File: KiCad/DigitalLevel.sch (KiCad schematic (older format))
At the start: 67 parts, among them SW1 SW_Push_Open, SW2 SW_Push_Open, SW3 SW_Push_Open, U2 MPU-6050, U3 XC6206P332MR

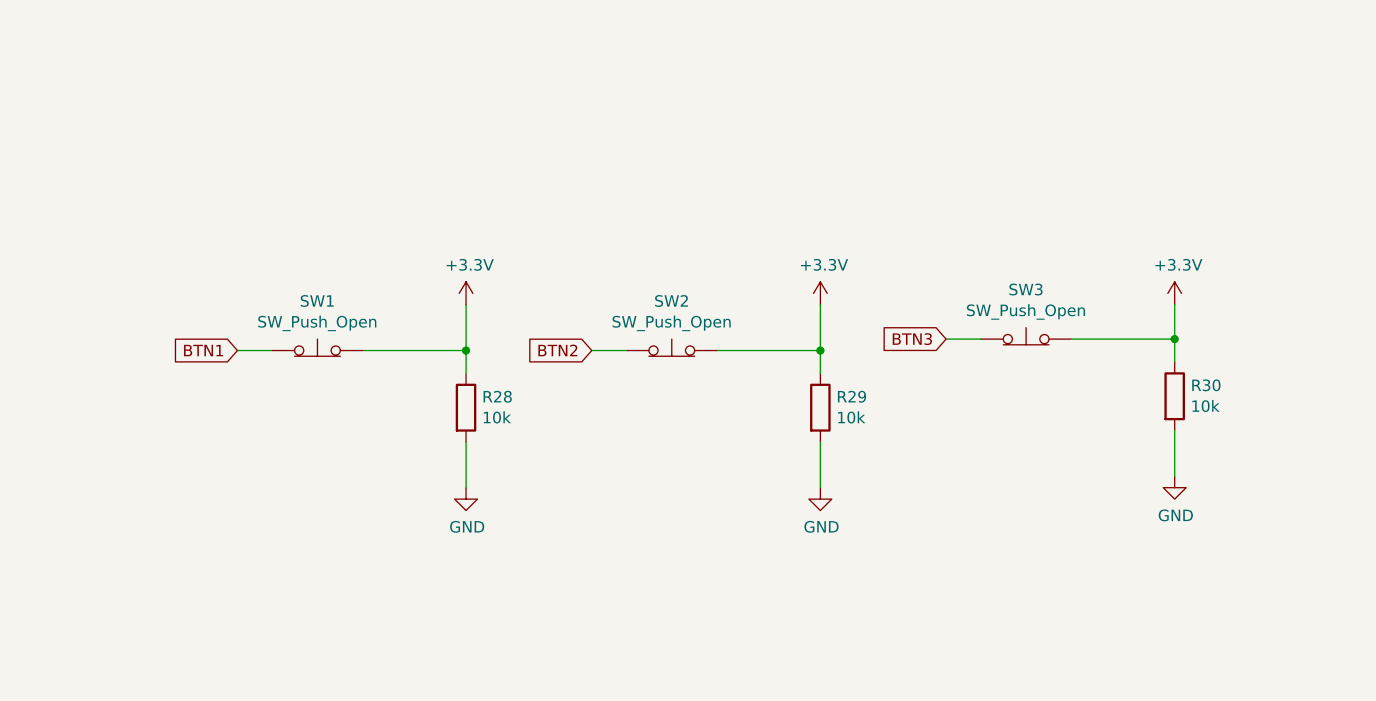
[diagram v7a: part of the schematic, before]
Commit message: Fixed schematics
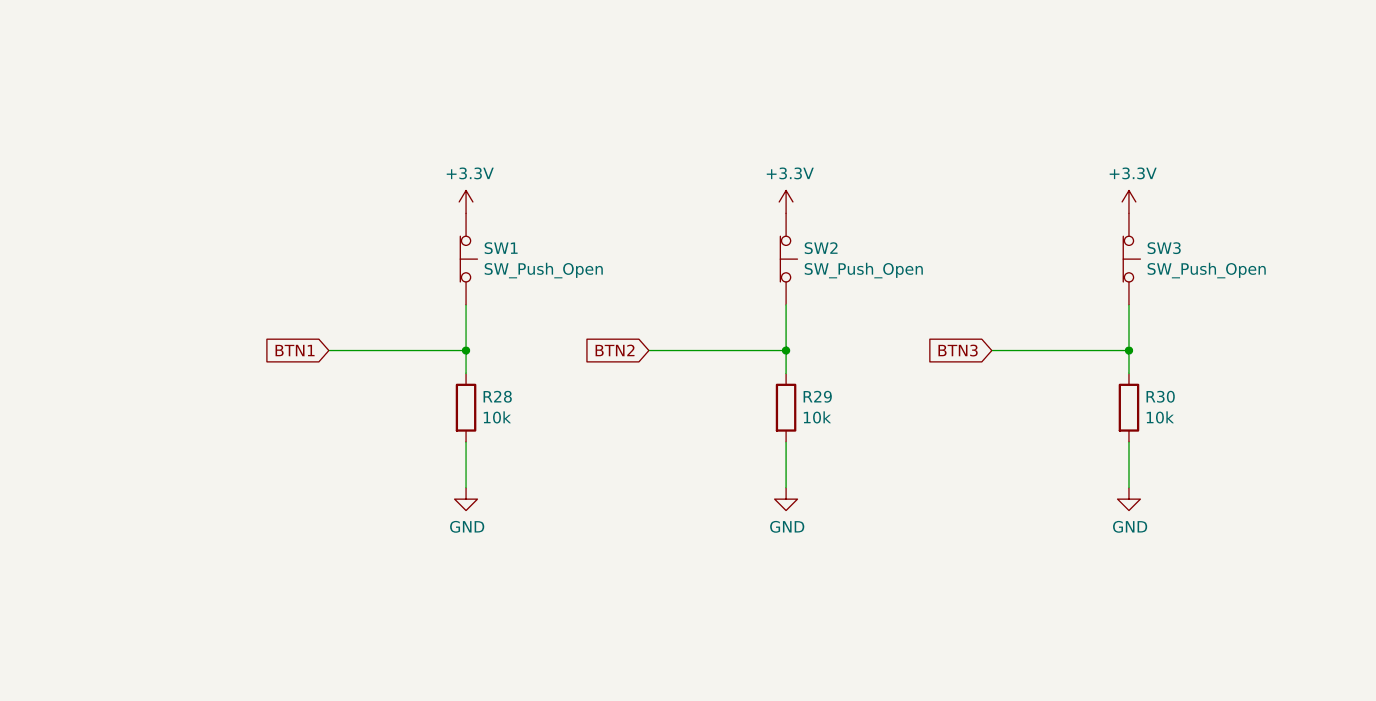
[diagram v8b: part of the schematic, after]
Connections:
- net +3V3: now also SW1.1 (A), SW2.1 (A), SW3.1 (A); no longer R28.1, R29.1, R30.1, SW1.2 (B), SW2.2 (B), SW3.2 (B)
- net BTN1: now also R28.1, SW1.2 (B); no longer SW1.1 (A)
- net BTN2: now also R29.1, SW2.2 (B); no longer SW2.1 (A)
- net BTN3: now also R30.1, SW3.2 (B); no longer SW3.1 (A)
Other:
- moved on the sheet: SW1
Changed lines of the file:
@@
 Wire Wire Line
 	1050 1700 1050 1850
-$Comp
-L Switch:SW_Push_Open SW2
-U 1 1 5E4F87F4
-P 7500 5600
-F 0 "SW2" H 7500 5815 50  0000 C CNN
-F 1 "SW_Push_Open" H 7500 5724 50  0000 C CNN
-F 2 "" H 7500 5800 50  0001 C CNN
-F 3 "~" H 7500 5800 50  0001 C CNN
-	1    7500 5600
-	1    0    0    -1
-$EndComp
-Wire Wire Line
-	8150 5600 7700 5600
-Wire Wire Line
-	8150 5600 8150 5700
-$Comp
-L Device:R R29
-U 1 1 5E52545B
-P 8150 5850
-F 0 "R29" H 8220 5896 50  0000 L CNN
-F 1 "10k" H 8220 5805 50  0000 L CNN
-F 2 "" V 8080 5850 50  0001 C CNN
-F 3 "~" H 8150 5850 50  0001 C CNN
-	1    8150 5850
-	1    0    0    -1
-$EndComp
-Wire Wire Line
-	8150 6000 8150 6200
-Wire Wire Line
-	7300 5600 7150 5600
-Text GLabel 7150 5600 0    50   Input ~ 0
-BTN2
 Text GLabel 2250 1000 1    50   Input ~ 0
 LED1
@@
 $EndComp
 $Comp
-L power:GND #PWR?
-U 1 1 5E599070
-P 8150 6200
-F 0 "#PWR?" H 8150 5950 50  0001 C CNN
-F 1 "GND" H 8155 6027 50  0000 C CNN
-F 2 "" H 8150 6200 50  0001 C CNN
-F 3 "" H 8150 6200 50  0001 C CNN
-	1    8150 6200
-	1    0    0    -1
-$EndComp
-Wire Wire Line
-	8150 5600 8150 5400
-Connection ~ 8150 5600
-$Comp
 L Switch:SW_Push_Open SW1
 U 1 1 5E5D8FE1
-P 5950 5600
-F 0 "SW1" H 5950 5815 50  0000 C CNN
-F 1 "SW_Push_Open" H 5950 5724 50  0000 C CNN
-F 2 "" H 5950 5800 50  0001 C CNN
-F 3 "~" H 5950 5800 50  0001 C CNN
-	1    5950 5600
-	1    0    0    -1
-$EndComp
-Wire Wire Line
-	6600 5600 6150 5600
+P 6600 5200
+F 0 "SW1" V 6554 5277 50  0000 L CNN
+F 1 "SW_Push_Open" V 6645 5277 50  0000 L CNN
+F 2 "" H 6600 5400 50  0001 C CNN
+F 3 "~" H 6600 5400 50  0001 C CNN
+	1    6600 5200
+	0    1    1    0
+$EndComp
 Wire Wire Line
 	6600 5600 6600 5700
@@
 Wire Wire Line
 	6600 6000 6600 6200
-Wire Wire Line
-	5750 5600 5600 5600
-Text GLabel 5600 5600 0    50   Input ~ 0
+Text GLabel 6000 5600 0    50   Input ~ 0
 BTN1
 $Comp
@@
 	6600 5600 6600 5400
 Connection ~ 6600 5600
-$Comp
-L Switch:SW_Push_Open SW3
-U 1 1 5E5E0331
-P 9050 5550
-F 0 "SW3" H 9050 5765 50  0000 C CNN
-F 1 "SW_Push_Open" H 9050 5674 50  0000 C CNN
-F 2 "" H 9050 5750 50  0001 C CNN
-F 3 "~" H 9050 5750 50  0001 C CNN
-	1    9050 5550
-	1    0    0    -1
-$EndComp
-Wire Wire Line
-	9700 5550 9250 5550
-Wire Wire Line
-	9700 5550 9700 5650
-$Comp
-L Device:R R30
-U 1 1 5E5E0339
-P 9700 5800
-F 0 "R30" H 9770 5846 50  0000 L CNN
-F 1 "10k" H 9770 5755 50  0000 L CNN
-F 2 "" V 9630 5800 50  0001 C CNN
-F 3 "~" H 9700 5800 50  0001 C CNN
-	1    9700 5800
-	1    0    0    -1
-$EndComp
-Wire Wire Line
-	9700 5950 9700 6150
-Wire Wire Line
-	8850 5550 8700 5550
-Text GLabel 8700 5550 0    50   Input ~ 0
-BTN3
-$Comp
-L power:GND #PWR?
-U 1 1 5E5E0348
-P 9700 6150
-F 0 "#PWR?" H 9700 5900 50  0001 C CNN
-F 1 "GND" H 9705 5977 50  0000 C CNN
-F 2 "" H 9700 6150 50  0001 C CNN
-F 3 "" H 9700 6150 50  0001 C CNN
-	1    9700 6150
-	1    0    0    -1
-$EndComp
 $Comp
 L power:GND #PWR?
@@
 $EndComp
 Wire Wire Line
-	9700 5400 9700 5550
-Connection ~ 9700 5550
-Wire Wire Line
 	8500 2700 8800 2700
 Wire Wire Line
@@
 L power:+3.3V #PWR?
 U 1 1 5E9B4D86
-P 6600 5400
-F 0 "#PWR?" H 6600 5250 50  0001 C CNN
-F 1 "+3.3V" H 6615 5573 50  0000 C CNN
-F 2 "" H 6600 5400 50  0001 C CNN
-F 3 "" H 6600 5400 50  0001 C CNN
-	1    6600 5400
-	1    0    0    -1
-$EndComp
-$Comp
-L power:+3.3V #PWR?
-U 1 1 5E9BB956
-P 8150 5400
-F 0 "#PWR?" H 8150 5250 50  0001 C CNN
-F 1 "+3.3V" H 8165 5573 50  0000 C CNN
-F 2 "" H 8150 5400 50  0001 C CNN
-F 3 "" H 8150 5400 50  0001 C CNN
-	1    8150 5400
-	1    0    0    -1
-$EndComp
-$Comp
-L power:+3.3V #PWR?
-U 1 1 5E9C25E4
-P 9700 5400
-F 0 "#PWR?" H 9700 5250 50  0001 C CNN
-F 1 "+3.3V" H 9715 5573 50  0000 C CNN
-F 2 "" H 9700 5400 50  0001 C CNN
-F 3 "" H 9700 5400 50  0001 C CNN
-	1    9700 5400
-	1    0    0    -1
-$EndComp
+P 6600 5000
+F 0 "#PWR?" H 6600 4850 50  0001 C CNN
+F 1 "+3.3V" H 6615 5173 50  0000 C CNN
+F 2 "" H 6600 5000 50  0001 C CNN
+F 3 "" H 6600 5000 50  0001 C CNN
+	1    6600 5000
+	1    0    0    -1
+$EndComp
+Wire Wire Line
+	6000 5600 6600 5600
+$Comp
+L Switch:SW_Push_Open SW2
+U 1 1 5EA01BE2
+P 8000 5200
+F 0 "SW2" V 7954 5277 50  0000 L CNN
+F 1 "SW_Push_Open" V 8045 5277 50  0000 L CNN
+F 2 "" H 8000 5400 50  0001 C CNN
+F 3 "~" H 8000 5400 50  0001 C CNN
+	1    8000 5200
+	0    1    1    0
+$EndComp
+Wire Wire Line
+	8000 5600 8000 5700
+$Comp
+L Device:R R29
+U 1 1 5EA01BE9
+P 8000 5850
+F 0 "R29" H 8070 5896 50  0000 L CNN
+F 1 "10k" H 8070 5805 50  0000 L CNN
+F 2 "" V 7930 5850 50  0001 C CNN
+F 3 "~" H 8000 5850 50  0001 C CNN
+	1    8000 5850
+	1    0    0    -1
+$EndComp
+Wire Wire Line
+	8000 6000 8000 6200
+Text GLabel 7400 5600 0    50   Input ~ 0
+BTN2
+$Comp
+L power:GND #PWR?
+U 1 1 5EA01BF1
+P 8000 6200
+F 0 "#PWR?" H 8000 5950 50  0001 C CNN
+F 1 "GND" H 8005 6027 50  0000 C CNN
+F 2 "" H 8000 6200 50  0001 C CNN
+F 3 "" H 8000 6200 50  0001 C CNN
+	1    8000 6200
+	1    0    0    -1
+$EndComp
+Wire Wire Line
+	8000 5600 8000 5400
+Connection ~ 8000 5600
+$Comp
+L power:+3.3V #PWR?
+U 1 1 5EA01BF9
+P 8000 5000
+F 0 "#PWR?" H 8000 4850 50  0001 C CNN
+F 1 "+3.3V" H 8015 5173 50  0000 C CNN
+F 2 "" H 8000 5000 50  0001 C CNN
+F 3 "" H 8000 5000 50  0001 C CNN
+	1    8000 5000
+	1    0    0    -1
+$EndComp
+Wire Wire Line
+	7400 5600 8000 5600
+$Comp
+L Switch:SW_Push_Open SW3
+U 1 1 5EA07F9B
+P 9500 5200
+F 0 "SW3" V 9454 5277 50  0000 L CNN
+F 1 "SW_Push_Open" V 9545 5277 50  0000 L CNN
+F 2 "" H 9500 5400 50  0001 C CNN
+F 3 "~" H 9500 5400 50  0001 C CNN
+	1    9500 5200
+	0    1    1    0
+$EndComp
+Wire Wire Line
+	9500 5600 9500 5700
+$Comp
+L Device:R R30
+U 1 1 5EA07FA2
+P 9500 5850
+F 0 "R30" H 9570 5896 50  0000 L CNN
+F 1 "10k" H 9570 5805 50  0000 L CNN
+F 2 "" V 9430 5850 50  0001 C CNN
+F 3 "~" H 9500 5850 50  0001 C CNN
+	1    9500 5850
+	1    0    0    -1
+$EndComp
+Wire Wire Line
+	9500 6000 9500 6200
+Text GLabel 8900 5600 0    50   Input ~ 0
+BTN3
+$Comp
+L power:GND #PWR?
+U 1 1 5EA07FAA
+P 9500 6200
+F 0 "#PWR?" H 9500 5950 50  0001 C CNN
+F 1 "GND" H 9505 6027 50  0000 C CNN
+F 2 "" H 9500 6200 50  0001 C CNN
+F 3 "" H 9500 6200 50  0001 C CNN
+	1    9500 6200
+	1    0    0    -1
+$EndComp
+Wire Wire Line
+	9500 5600 9500 5400
+Connection ~ 9500 5600
+$Comp
+L power:+3.3V #PWR?
+U 1 1 5EA07FB2
+P 9500 5000
+F 0 "#PWR?" H 9500 4850 50  0001 C CNN
+F 1 "+3.3V" H 9515 5173 50  0000 C CNN
+F 2 "" H 9500 5000 50  0001 C CNN
+F 3 "" H 9500 5000 50  0001 C CNN
+	1    9500 5000
+	1    0    0    -1
+$EndComp
+Wire Wire Line
+	8900 5600 9500 5600
 $EndSCHEMATC
